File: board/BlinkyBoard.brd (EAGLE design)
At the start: 33 x 12.2 mm, 17 parts, among them Q1 16 MHz

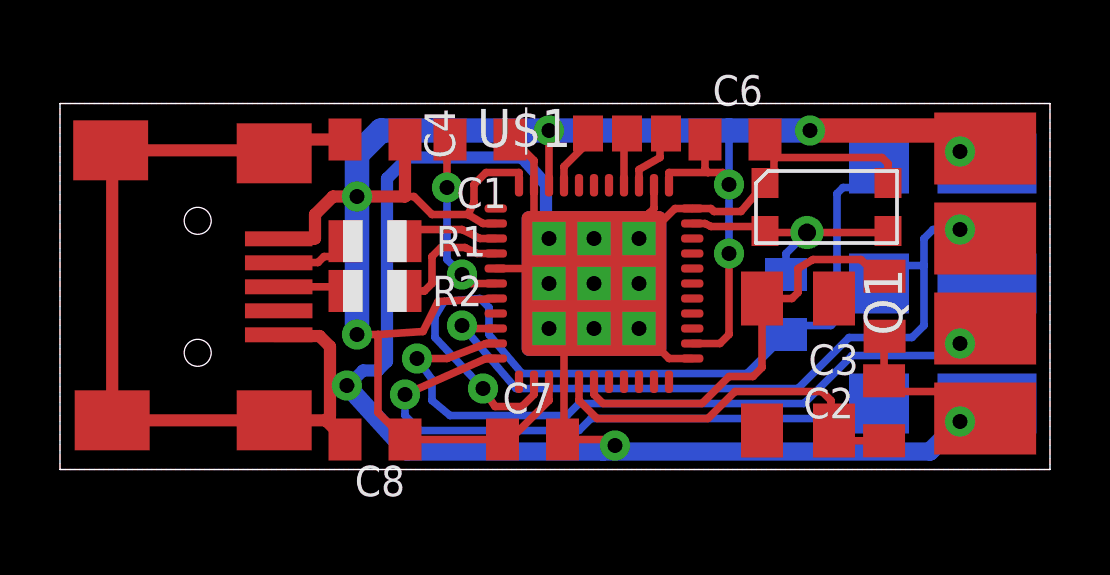
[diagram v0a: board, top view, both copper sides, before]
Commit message: Add silk, make ground trace wider, rename to BlinkyBoard
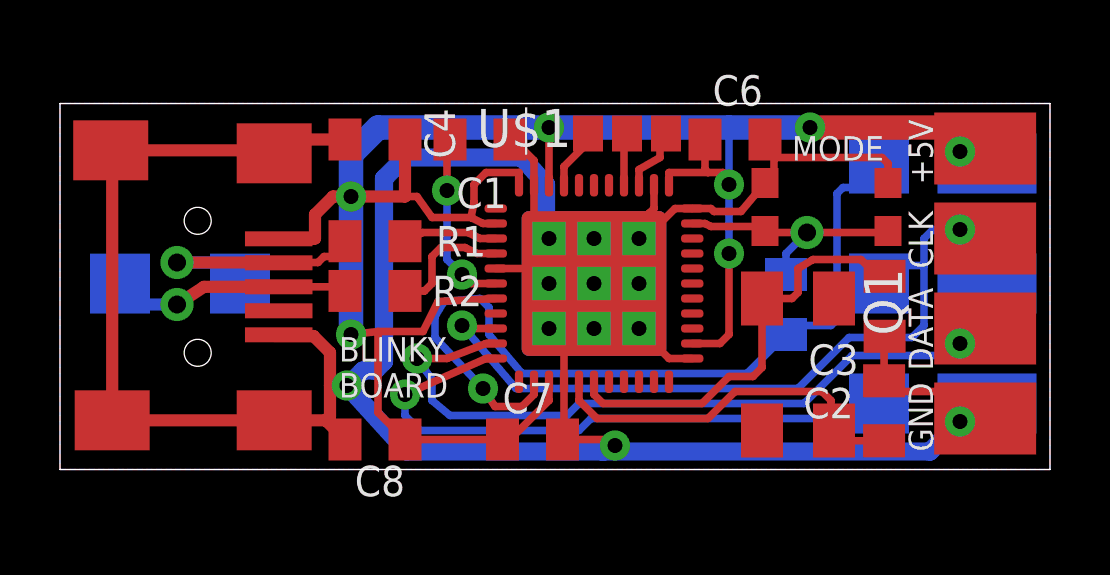
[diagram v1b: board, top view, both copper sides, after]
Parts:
- added U$2: GLOWBOARD_USB_TEST_PADS, blinkyboard:GLOWBOARD_USB_TEST_PADS
- R1, R2: device adafruit:R0805 -> blinkyboard:ADAFRUIT_R0805
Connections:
- removed net N$2: R2.1, U$6.P$3
- removed net N$5: R1.1, U$6.P$2
- new net D+_IN: R2.1, U$2.D+, U$6.P$3
- new net D-_IN: R1.1, U$2.D-, U$6.P$2
- net SCK: now also U$4.SCK; no longer U$4.SCK`
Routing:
- net D-_IN: track 0.00 -> 8.96 mm, vias 0 -> 1
- net D+_IN: track 0.00 -> 8.66 mm, vias 0 -> 1
- net N$5: track 3.37 -> 0.00 mm
- net N$2: track 2.50 -> 0.00 mm
- net VCC: track 71.3 -> 72.3 mm
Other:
- board text added: "+5V"
- board text added: "9/9/2012"
- board text added: "BLINKY"
- board text added: "BOARD"
- board text added: "CLK"
- board text added: "D+"
- board text added: "D-"
- board text added: "DATA"
- board text added: "GND"
- board text added: "MISO"
- board text added: "MODE"
- board text added: "MOSI"
- board text added: "RST"
- board text added: "Rev A"
- board text added: "SCK"
- board text added: "VCC"
